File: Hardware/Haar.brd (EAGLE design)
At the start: 29.1 x 10.1 mm, 15 parts, among them J1 CONN_42.54, Q1 2N7002, U1 SHT35DFN, U2 LPS35HW, U4 TPS62237DRY, U5 TXS0102DQM

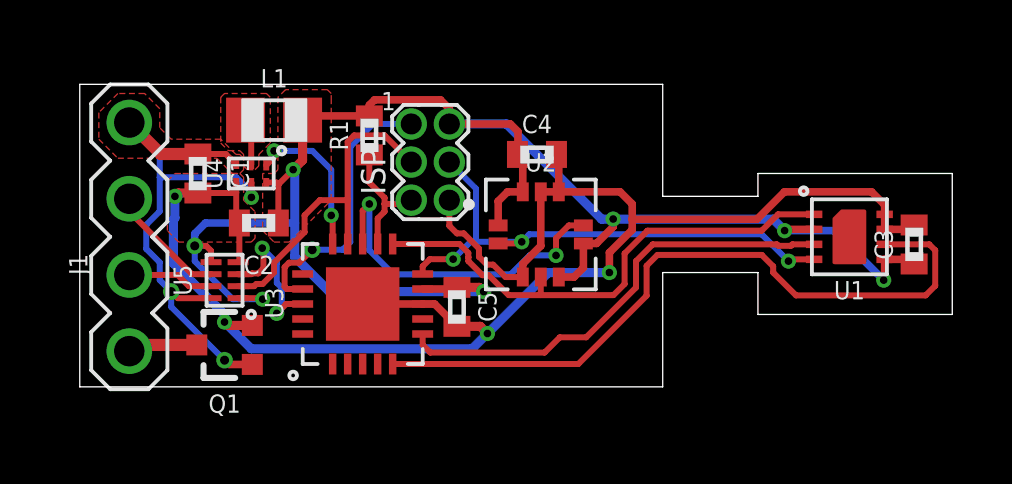
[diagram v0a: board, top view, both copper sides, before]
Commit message: Fixed ISP error, updated notes
Fixed an errant connection to the ISP header on both versions in schematic, still need to fix the layout. Also removed outdated notes on schematic
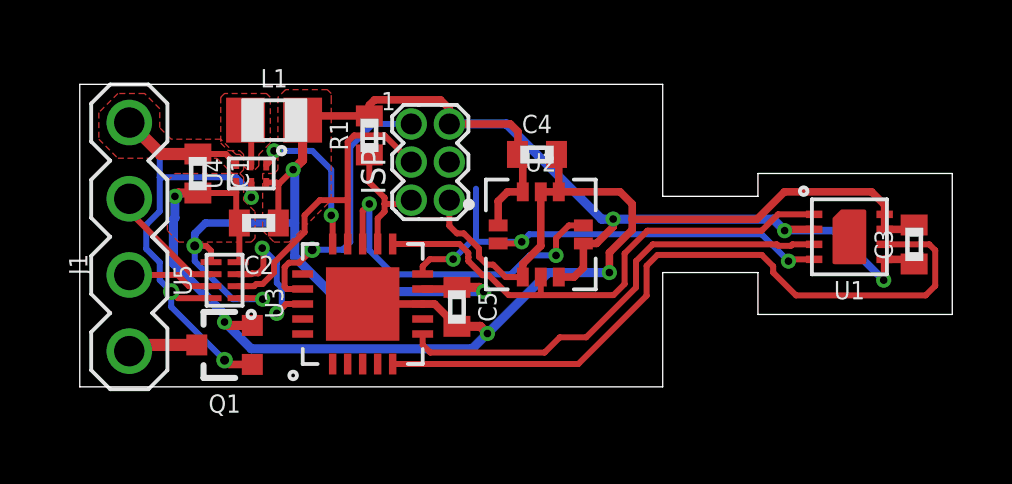
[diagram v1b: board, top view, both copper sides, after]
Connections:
- net SCL: no longer ISP1.4
- net SDA_EXT: now also ISP1.4
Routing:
- net SCL: track 18.0 -> 16.7 mm
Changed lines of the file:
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@@
 <vertex x="1.27" y="7.62"/>
-<vertex x="4.572" y="7.62"/>
 <vertex x="4.572" y="7.62"/>
 <vertex x="5.08" y="7.112"/>
@@
 <wire x1="6.731" y1="3.302" x2="6.731" y2="2.6127375" width="0.2" layer="16"/>
 <wire x1="6.731" y1="2.6127375" x2="6.56763125" y2="2.44936875" width="0.2" layer="16"/>
+<contactref element="ISP1" pad="4"/>
+<wire x1="6.56763125" y1="4.13731875" x2="12.319" y2="7.493" width="0" layer="19" extent="16-16"/>
 </signal>
 <signal name="RX">
@@
 <contactref element="U1" pad="4"/>
 <contactref element="U2" pad="2"/>
-<contactref element="ISP1" pad="4"/>
 <wire x1="11.6696" y1="4.2556" x2="11.43" y2="4.016" width="0.2" layer="1"/>
 <wire x1="11.43" y1="3.762" x2="11.43" y2="4.016" width="0.2" layer="1"/>
@@
 <wire x1="23.622" y1="4.191" x2="23.681" y2="4.25" width="0.2" layer="1"/>
 <wire x1="23.681" y1="4.25" x2="24.479" y2="4.25" width="0.2" layer="1"/>
-<wire x1="12.319" y1="7.493" x2="13.208" y2="6.604" width="0.2" layer="16"/>
 <wire x1="13.208" y1="6.604" x2="13.208" y2="4.834" width="0.2" layer="16"/>
 </signal>
